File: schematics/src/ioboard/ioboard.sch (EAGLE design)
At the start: 32 parts, among them IC1 TL072P, IC2 TL072P, IC3 TL072P

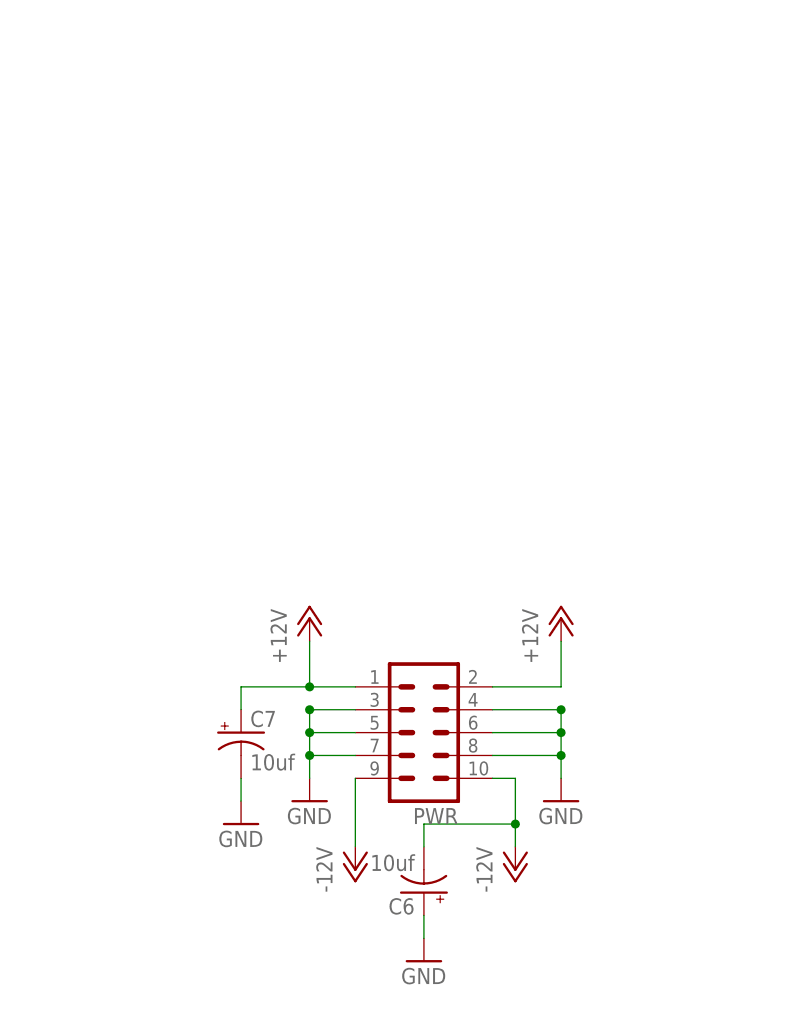
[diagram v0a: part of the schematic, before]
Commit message: Updated Schematics, Fixed Power Socket orientation
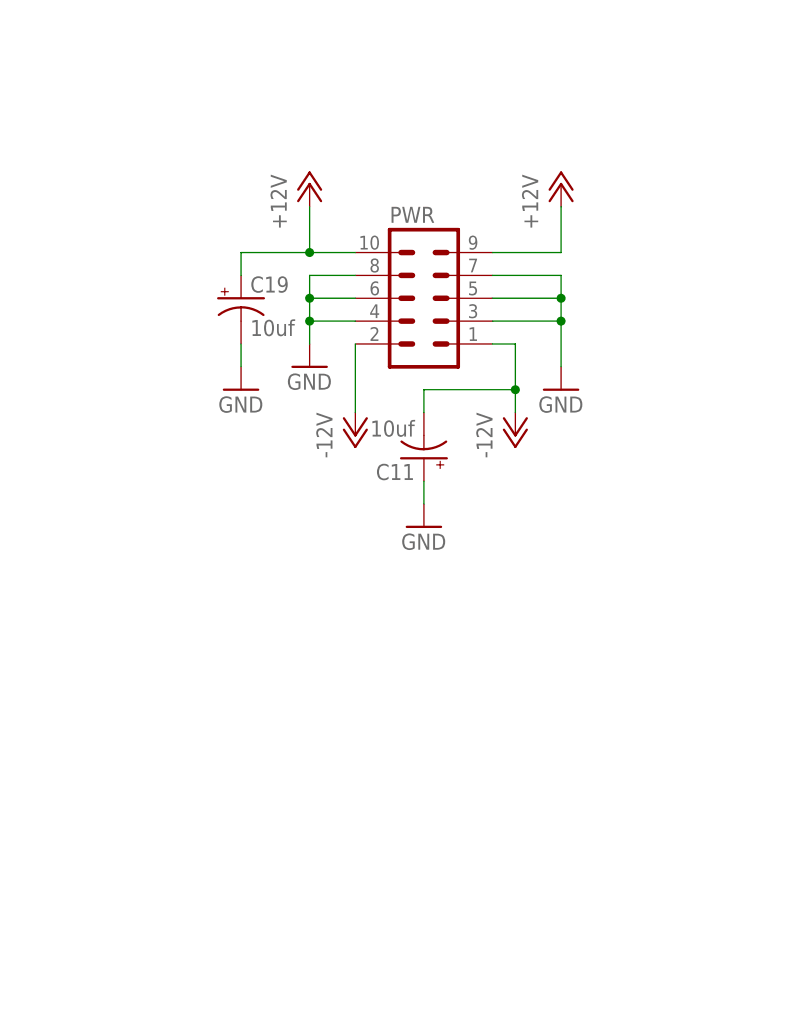
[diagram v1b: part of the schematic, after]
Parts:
- removed C6, C7: 10uf, resistor:CPOL-USE2.5-5
- added C11, C19: 10uf, resistor:CPOL-USE2.5-5
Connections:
- net +12V: now also C19.+, PWR.10, PWR.9; no longer C7.+, PWR.1, PWR.2
- net -12V: now also C11.-, PWR.1, PWR.2; no longer C6.-, PWR.10, PWR.9
- net GND: now also C11.+, C19.-; no longer C6.+, C7.-
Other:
- moved on the sheet: PWR
